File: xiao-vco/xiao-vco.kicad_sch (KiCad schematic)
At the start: 49 parts, among them J1 C2M, J2 C2F, J3 Eurorack Power, J4 CV1, J5 V/OCT, J6 OUT, J7 CV2, J8 C1M, J9 C1F, U1 SeeeduinoXIAO, U2 MCP6004, U3 LM4040DBZ-10, U4 TL072, U5 LM1117-5.0

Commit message: First completed routing
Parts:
- RV1: footprint Potentiometer_THT:Potentiometer_Alpha_RD901F-40-00D_Single_Vertical -> Personal:Potentiometer_Alpha_RD901F-40-00D_Single_Vertical-Hanging
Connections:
- net GND: no longer C1.2, C2.2, C3.2, C4.2, J2.1 (Pin_1), J4.S, J5.S, J6.S, J7.S, J9.1 (Pin_1), RV1.1, RV2.1, RV3.1, RV4.1
- new net GND1: C1.2, C2.2, C3.2, C4.2, J2.1 (Pin_1), J4.S, J5.S, J6.S, J7.S, J9.1 (Pin_1), RV1.1, RV2.1, RV3.1, RV4.1
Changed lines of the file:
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@@
     (pin "2")
-  )
-  (symbol (lib_name "GND_22") (lib_id "power:GND") (at 86.36 177.165 0) (unit 1)
-    (in_bom yes) (on_board yes) (fields_autoplaced)
-    (property "Reference" "#PWR0101" (id 0) (at 86.36 183.515 0)
-      (effects (font (size 1.27 1.27)) hide)
-    )
-    (property "Value" "GND" (id 1) (at 86.36 181.61 0))
-    (property "Footprint" "" (id 2) (at 86.36 177.165 0)
-      (effects (font (size 1.27 1.27)) hide)
-    )
-    (property "Datasheet" "" (id 3) (at 86.36 177.165 0)
-      (effects (font (size 1.27 1.27)) hide)
-    )
-    (pin "1")
   )
   (symbol (lib_id "Amplifier_Operational:MCP6004") (at 340.995 222.25 0) (mirror x) (unit 4)
@@
     (pin "1")
   )
+  (symbol (lib_id "power:GND1") (at 327.66 173.355 0) (unit 1)
+    (in_bom yes) (on_board yes) (fields_autoplaced)
+    (property "Reference" "#PWR?" (id 0) (at 327.66 179.705 0)
+      (effects (font (size 1.27 1.27)) hide)
+    )
+    (property "Value" "GND1" (id 1) (at 327.66 177.8 0))
+    (property "Footprint" "" (id 2) (at 327.66 173.355 0)
+      (effects (font (size 1.27 1.27)) hide)
+    )
+    (property "Datasheet" "" (id 3) (at 327.66 173.355 0)
+      (effects (font (size 1.27 1.27)) hide)
+    )
+    (pin "1")
+  )
   (symbol (lib_id "Connector:AudioJack2_SwitchT") (at 302.895 147.32 0) (mirror x) (unit 1)
     (in_bom yes) (on_board yes) (fields_autoplaced)
@@
     (pin "1")
   )
-  (symbol (lib_name "GND_22") (lib_id "power:GND") (at 327.66 173.355 0) (unit 1)
-    (in_bom yes) (on_board yes) (fields_autoplaced)
-    (property "Reference" "#PWR0102" (id 0) (at 327.66 179.705 0)
-      (effects (font (size 1.27 1.27)) hide)
-    )
-    (property "Value" "GND" (id 1) (at 327.66 177.8 0))
-    (property "Footprint" "" (id 2) (at 327.66 173.355 0)
-      (effects (font (size 1.27 1.27)) hide)
-    )
-    (property "Datasheet" "" (id 3) (at 327.66 173.355 0)
-      (effects (font (size 1.27 1.27)) hide)
-    )
-    (pin "1")
-  )
   (symbol (lib_name "GND_3") (lib_id "power:GND") (at 234.315 64.77 90) (unit 1)
     (in_bom yes) (on_board yes) (fields_autoplaced)
@@
       (effects (font (size 1.27 1.27)) (justify right))
     )
-    (property "Footprint" "Potentiometer_THT:Potentiometer_Alpha_RD901F-40-00D_Single_Vertical" (id 2) (at 57.785 186.69 0)
+    (property "Footprint" "Personal:Potentiometer_Alpha_RD901F-40-00D_Single_Vertical-Hanging" (id 2) (at 57.785 186.69 0)
       (effects (font (size 1.27 1.27)) hide)
     )
@@
     (pin "1")
     (pin "2")
+  )
+  (symbol (lib_id "power:GND1") (at 86.36 177.165 0) (unit 1)
+    (in_bom yes) (on_board yes) (fields_autoplaced)
+    (property "Reference" "#PWR?" (id 0) (at 86.36 183.515 0)
+      (effects (font (size 1.27 1.27)) hide)
+    )
+    (property "Value" "GND1" (id 1) (at 86.36 181.61 0))
+    (property "Footprint" "" (id 2) (at 86.36 177.165 0)
+      (effects (font (size 1.27 1.27)) hide)
+    )
+    (property "Datasheet" "" (id 3) (at 86.36 177.165 0)
+      (effects (font (size 1.27 1.27)) hide)
+    )
+    (pin "1")
   )
   (symbol (lib_id "Amplifier_Operational:MCP6004") (at 188.595 222.885 0) (unit 2)
@@
       (reference "#PWR031") (unit 1) (value "+12V") (footprint "")
     )
-    (path "/7316d701-2e9d-4468-b1bd-dd674ed2a841"
-      (reference "#PWR0101") (unit 1) (value "GND") (footprint "")
-    )
-    (path "/bc2ec25b-e2f5-46be-9c1f-386b82895f1f"
-      (reference "#PWR0102") (unit 1) (value "GND") (footprint "")
+    (path "/81fa7b9b-1048-4ab6-96a4-17bbea9ee926"
+      (reference "#PWR?") (unit 1) (value "GND1") (footprint "")
+    )
+    (path "/db50dabe-48fe-48c9-b18b-8fbca1cd1c84"
+      (reference "#PWR?") (unit 1) (value "GND1") (footprint "")
     )
     (path "/20e08b86-fdfe-4f67-ab5d-3979aed36888"
@@
     )
     (path "/c0c58b3a-1fc2-402f-86a6-7e316c0c5aa5"
-      (reference "RV1") (unit 1) (value "B10k") (footprint "Potentiometer_THT:Potentiometer_Alpha_RD901F-40-00D_Single_Vertical")
+      (reference "RV1") (unit 1) (value "B10k") (footprint "Personal:Potentiometer_Alpha_RD901F-40-00D_Single_Vertical-Hanging")
     )
     (path "/2cdd6a82-e941-4486-beed-3870aaf79794"

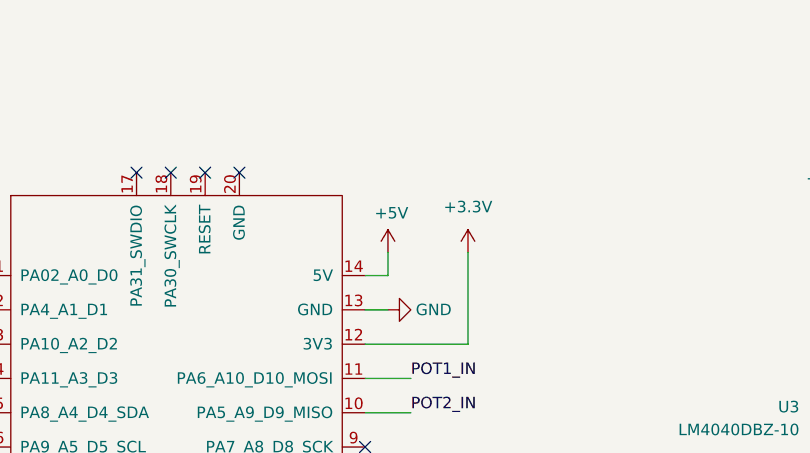
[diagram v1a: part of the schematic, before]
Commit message: Routed all on one face
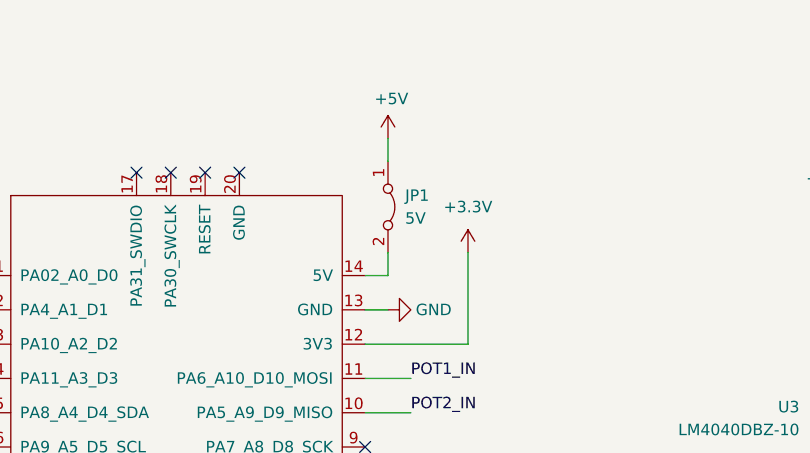
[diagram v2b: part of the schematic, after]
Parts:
- added JP1: 5V, Connector_PinHeader_2.54mm:PinHeader_1x02_P2.54mm_Vertical, symbol Jumper:Jumper_2_Bridged
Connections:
- net +5V: now also JP1.1 (A); no longer U1.14 (5V)
- new net: JP1.2 (B), U1.14 (5V)
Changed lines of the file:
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@@
+    (stroke (width 0) (type default) (color 0 0 0 0))
+  )
+  (wire (pts (xy 106.68 36.83) (xy 106.68 39.37))
     (stroke (width 0) (type default) (color 0 0 0 0))
   )
@@
     (pin "1")
   )
-  (symbol (lib_id "power:+5V") (at 106.68 49.53 0) (unit 1)
+  (symbol (lib_id "power:+5V") (at 106.68 36.83 0) (unit 1)
     (in_bom yes) (on_board yes)
-    (property "Reference" "#PWR04" (id 0) (at 106.68 53.34 0)
-      (effects (font (size 1.27 1.27)) hide)
-    )
-    (property "Value" "+5V" (id 1) (at 107.061 45.1358 0))
-    (property "Footprint" "" (id 2) (at 106.68 49.53 0)
-      (effects (font (size 1.27 1.27)) hide)
-    )
-    (property "Datasheet" "" (id 3) (at 106.68 49.53 0)
+    (property "Reference" "#PWR04" (id 0) (at 106.68 40.64 0)
+      (effects (font (size 1.27 1.27)) hide)
+    )
+    (property "Value" "+5V" (id 1) (at 107.061 32.4358 0))
+    (property "Footprint" "" (id 2) (at 106.68 36.83 0)
+      (effects (font (size 1.27 1.27)) hide)
+    )
+    (property "Datasheet" "" (id 3) (at 106.68 36.83 0)
       (effects (font (size 1.27 1.27)) hide)
     )
@@
     (pin "1")
   )
+  (symbol (lib_id "Jumper:Jumper_2_Bridged") (at 106.68 44.45 270) (unit 1)
+    (in_bom yes) (on_board yes) (fields_autoplaced)
+    (property "Reference" "JP1" (id 0) (at 108.585 43.1799 90)
+      (effects (font (size 1.27 1.27)) (justify left))
+    )
+    (property "Value" "5V" (id 1) (at 108.585 45.7199 90)
+      (effects (font (size 1.27 1.27)) (justify left))
+    )
+    (property "Footprint" "Connector_PinHeader_2.54mm:PinHeader_1x02_P2.54mm_Vertical" (id 2) (at 106.68 44.45 0)
+      (effects (font (size 1.27 1.27)) hide)
+    )
+    (property "Datasheet" "~" (id 3) (at 106.68 44.45 0)
+      (effects (font (size 1.27 1.27)) hide)
+    )
+    (pin "1")
+    (pin "2")
+  )
   (symbol (lib_name "R_8") (lib_id "Device:R") (at 86.36 231.775 90) (unit 1)
     (in_bom yes) (on_board yes)
@@
   (symbol (lib_id "power:GND1") (at 327.66 173.355 0) (unit 1)
     (in_bom yes) (on_board yes) (fields_autoplaced)
-    (property "Reference" "#PWR?" (id 0) (at 327.66 179.705 0)
+    (property "Reference" "#PWR0102" (id 0) (at 327.66 179.705 0)
       (effects (font (size 1.27 1.27)) hide)
     )
@@
   (symbol (lib_id "power:GND1") (at 86.36 177.165 0) (unit 1)
     (in_bom yes) (on_board yes) (fields_autoplaced)
-    (property "Reference" "#PWR?" (id 0) (at 86.36 183.515 0)
+    (property "Reference" "#PWR0101" (id 0) (at 86.36 183.515 0)
       (effects (font (size 1.27 1.27)) hide)
     )
@@
       (reference "#PWR031") (unit 1) (value "+12V") (footprint "")
     )
+    (path "/db50dabe-48fe-48c9-b18b-8fbca1cd1c84"
+      (reference "#PWR0101") (unit 1) (value "GND1") (footprint "")
+    )
     (path "/81fa7b9b-1048-4ab6-96a4-17bbea9ee926"
-      (reference "#PWR?") (unit 1) (value "GND1") (footprint "")
-    )
-    (path "/db50dabe-48fe-48c9-b18b-8fbca1cd1c84"
-      (reference "#PWR?") (unit 1) (value "GND1") (footprint "")
+      (reference "#PWR0102") (unit 1) (value "GND1") (footprint "")
     )
     (path "/20e08b86-fdfe-4f67-ab5d-3979aed36888"
@@
       (reference "J9") (unit 1) (value "C1F") (footprint "Connector_PinSocket_2.54mm:PinSocket_1x06_P2.54mm_Vertical")
     )
+    (path "/3342ba43-82dc-4741-934c-4dcfb7976118"
+      (reference "JP1") (unit 1) (value "5V") (footprint "Connector_PinHeader_2.54mm:PinHeader_1x02_P2.54mm_Vertical")
+    )
     (path "/6c8c0289-6b78-4da5-98e2-9b7639f150b3"

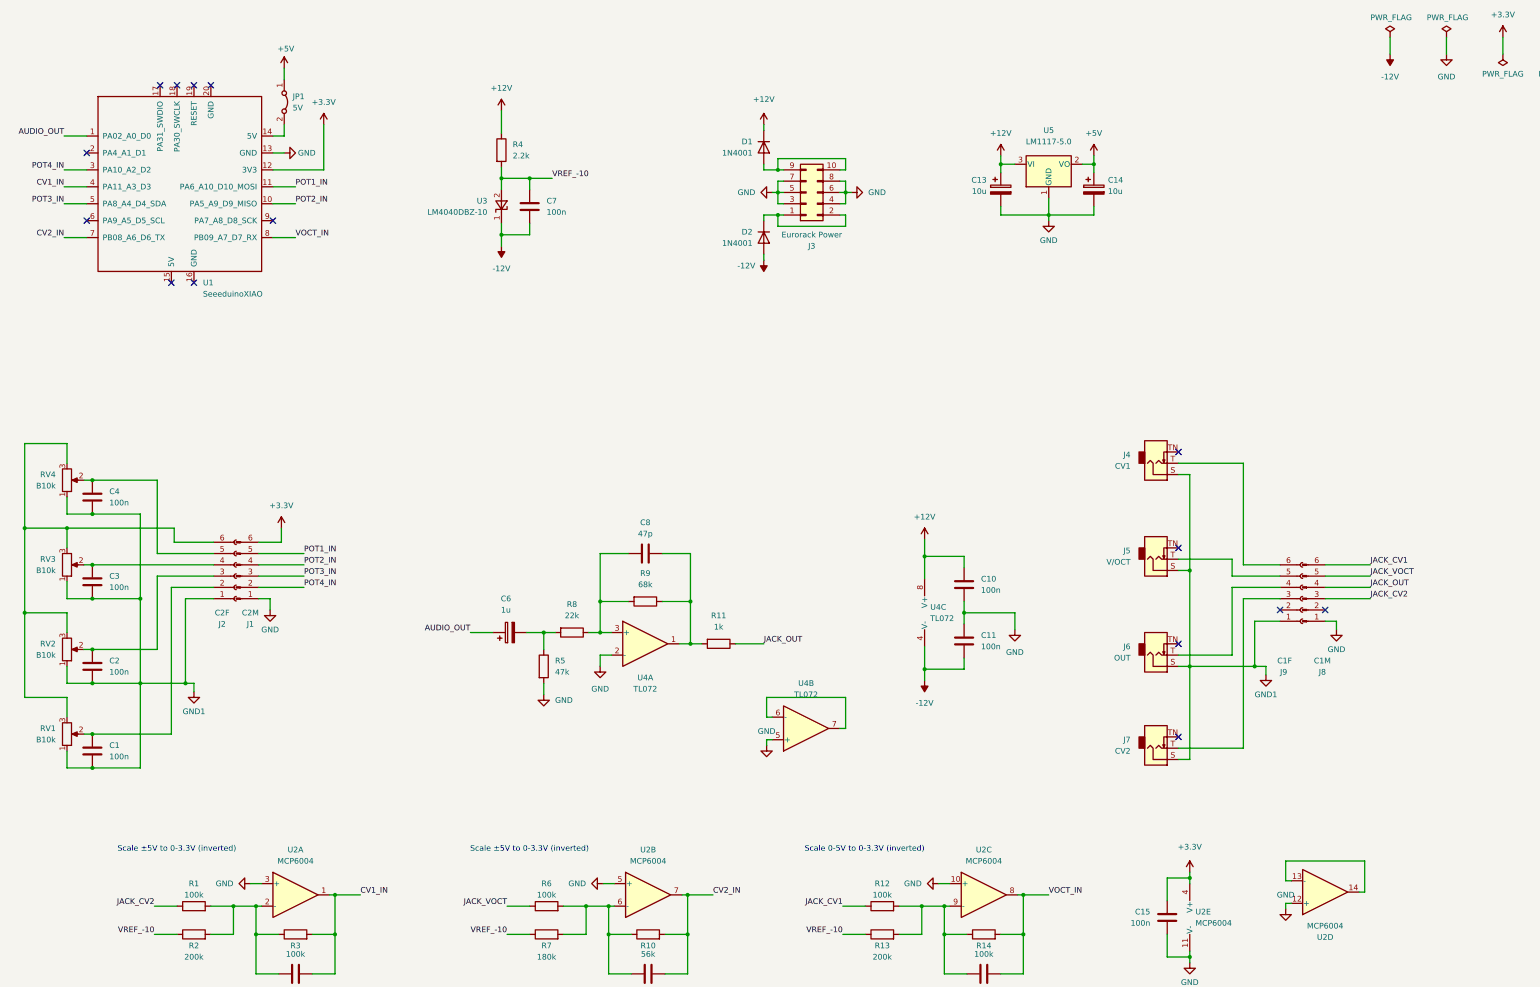
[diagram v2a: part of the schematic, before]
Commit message: Components now face inwards
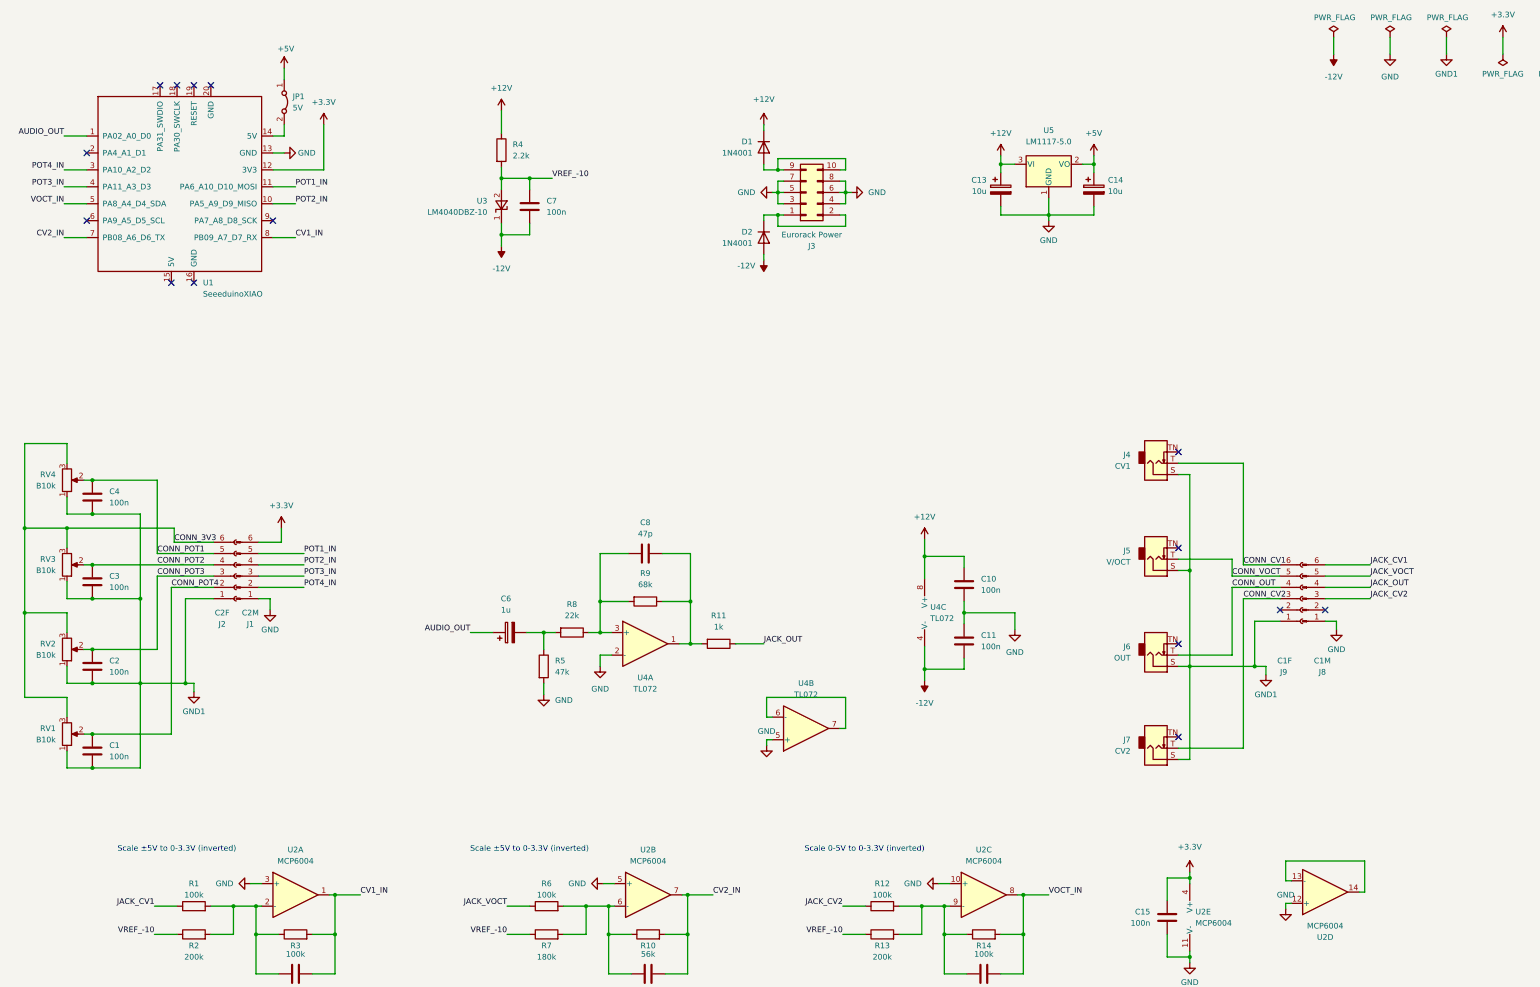
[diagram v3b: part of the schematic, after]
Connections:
- net CV1_IN: now also U1.8 (PB09_A7_D7_RX); no longer U1.4 (PA11_A3_D3)
- net JACK_CV1: now also R1.1; no longer R12.1
- net JACK_CV2: now also R12.1; no longer R1.1
- net POT3_IN: now also U1.4 (PA11_A3_D3); no longer U1.5 (PA8_A4_D4_SDA)
- net VOCT_IN: now also U1.5 (PA8_A4_D4_SDA); no longer U1.8 (PB09_A7_D7_RX)
- net CONN_POT1: now reaches C4.1, J2.5 (Pin_5), RV4.2
- net CONN_3V3: now reaches J2.6 (Pin_6), RV1.3, RV2.3, RV3.3, RV4.3
- net CONN_POT4: now reaches C1.1, J2.2 (Pin_2), RV1.2
- net CONN_POT3: now reaches C2.1, J2.3 (Pin_3), RV2.2
- net CONN_CV1: now reaches J4.T, J9.6 (Pin_6)
- net CONN_VOCT: now reaches J5.T, J9.5 (Pin_5)
- net CONN_CV2: now reaches J7.T, J9.3 (Pin_3)
- net CONN_OUT: now reaches J6.T, J9.4 (Pin_4)
- net CONN_POT2: now reaches C3.1, J2.4 (Pin_4), RV3.2

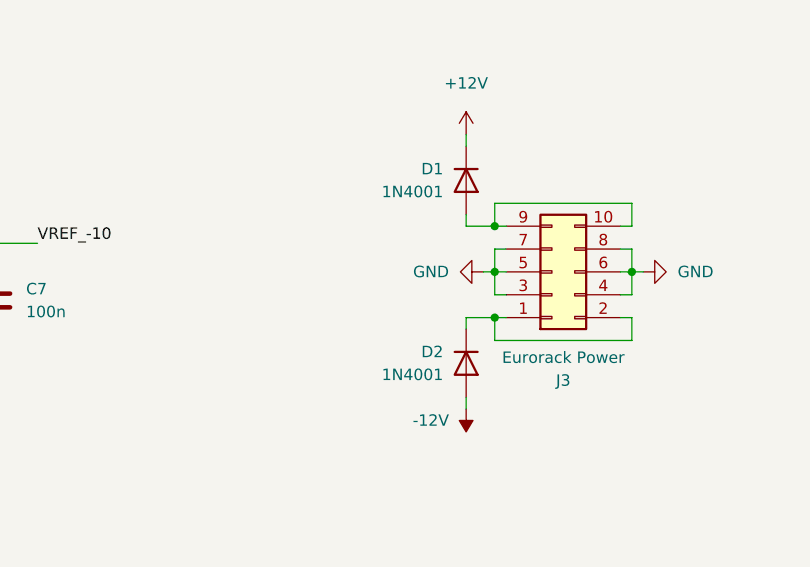
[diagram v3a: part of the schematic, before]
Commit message: Use SMD diodes
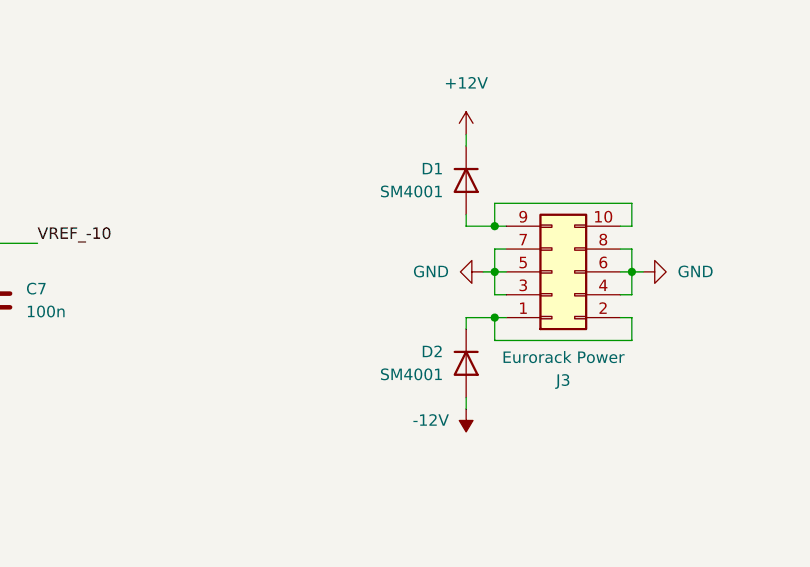
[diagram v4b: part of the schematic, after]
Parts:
- C1, C10, C11, C15, C2, C3, C4, C7: LCSC (none) -> C14663
- C12, C8, C9: LCSC (none) -> C1671
- D1, D2: value 1N4001 -> SM4001; footprint Diode_THT:D_DO-41_SOD81_P10.16mm_Horizontal -> Personal:SOD-123FL; LCSC (none) -> C64898
- J3: footprint Custom_Footprints:Eurorack_10_pin_header -> Personal:Eurorack_10_pin_header
- R1, R12, R14, R3, R6: LCSC (none) -> C25803
- R10: LCSC (none) -> C23206
- R11: LCSC (none) -> C21190
- R13, R2: LCSC (none) -> C25811
- R4: LCSC (none) -> C4190
- R5: LCSC (none) -> C25819
- R7: LCSC (none) -> C22827
- R8: LCSC (none) -> C31850
- R9: LCSC (none) -> C23231
- U4: footprint Package_SO:SOIC-8_3.9x4.9mm_P1.27mm -> Package_SO:SOIC-14_3.9x8.7mm_P1.27mm; LCSC (none) -> C6961
- U4: footprint Package_SO:SOIC-8_3.9x4.9mm_P1.27mm -> Package_SO:SOIC-14_3.9x8.7mm_P1.27mm
